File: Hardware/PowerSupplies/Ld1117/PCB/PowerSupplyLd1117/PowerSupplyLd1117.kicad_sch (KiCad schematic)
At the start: 6 parts, among them J1 Conn_01x02_Pin, J2 Barrel_Jack, U1 LM7805_TO220

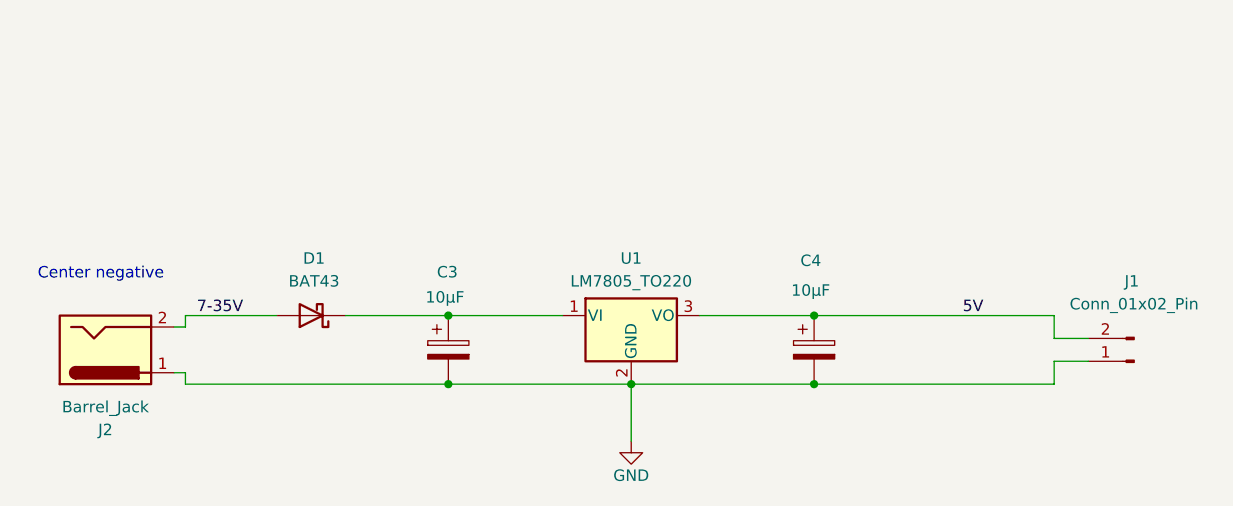
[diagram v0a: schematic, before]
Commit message: power supplies added
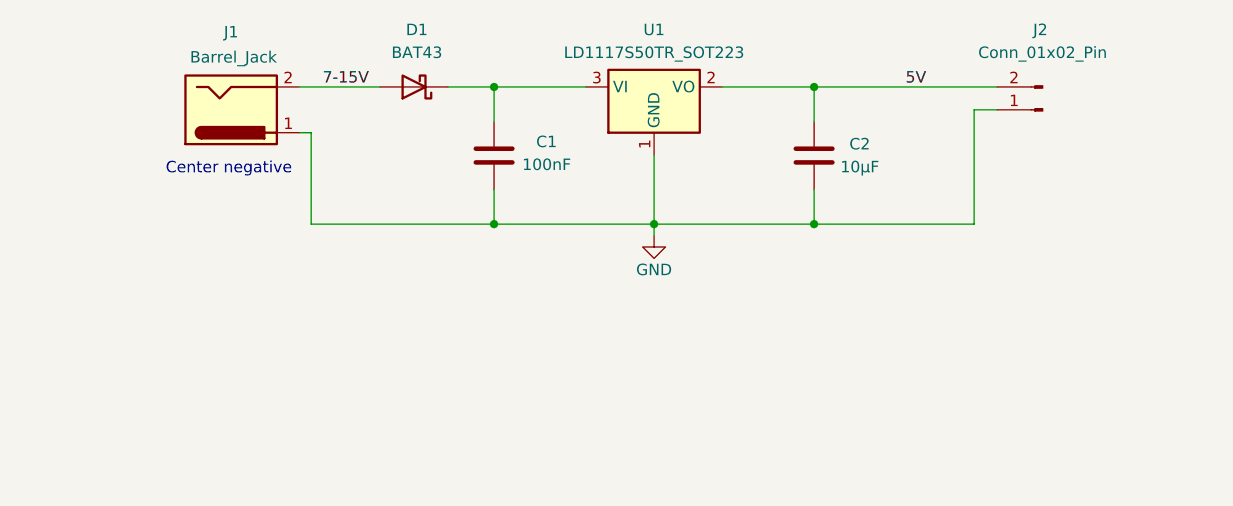
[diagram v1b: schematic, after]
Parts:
- removed C3, C4: 10μF, Capacitor_THT:C_Radial_D6.3mm_H7.0mm_P2.50mm, symbol Device:C_Polarized
- removed J1: Conn_01x02_Pin, Connector_PinSocket_2.54mm:PinSocket_1x02_P2.54mm_Horizontal, symbol Connector:Conn_01x02_Pin
- removed J2: Barrel_Jack, Connector_BarrelJack:BarrelJack_GCT_DCJ200-10-A_Horizontal, symbol Connector:Barrel_Jack
- removed U1: LM7805_TO220, Package_TO_SOT_THT:TO-220-3_Vertical, symbol Regulator_Linear:LM7805_TO220
- added C1: 100nF, Capacitor_THT:C_Disc_D5.0mm_W2.5mm_P2.50mm, symbol Device:C
- added C2: 10μF, Capacitor_THT:C_Disc_D5.0mm_W2.5mm_P5.00mm, symbol Device:C
- added J1: Barrel_Jack, Connector_BarrelJack:BarrelJack_GCT_DCJ200-10-A_Horizontal, symbol Connector:Barrel_Jack
- added J2: Conn_01x02_Pin, Connector_PinSocket_2.54mm:PinSocket_1x02_P2.54mm_Horizontal, symbol Connector:Conn_01x02_Pin
- added U1: LD1117S50TR_SOT223, Package_TO_SOT_SMD:SOT-223-3_TabPin2, symbol Regulator_Linear:LD1117S50TR_SOT223
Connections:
- net 5V: now also C2.1, J2.2 (Pin_2), U1.2 (VO)
- net GND: now also C1.2, C2.2, J1.1, J2.1 (Pin_1), U1.1 (GND)
- net at D1.1 (K): now also C1.1, U1.3 (VI)
- net 7-35V renamed 7-15V
- net 7-15V: now also J1.2
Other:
- title: Daisy Seed Development Kit Power Supply LM7805 -> (none)
